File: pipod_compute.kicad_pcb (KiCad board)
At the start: 4 copper layers, 55.5 x 84.8 mm, 37 parts, among them J1 Micro_SD_Card, J2 S7041-42R, J3 S7041-42R, J5 2-1734839-5

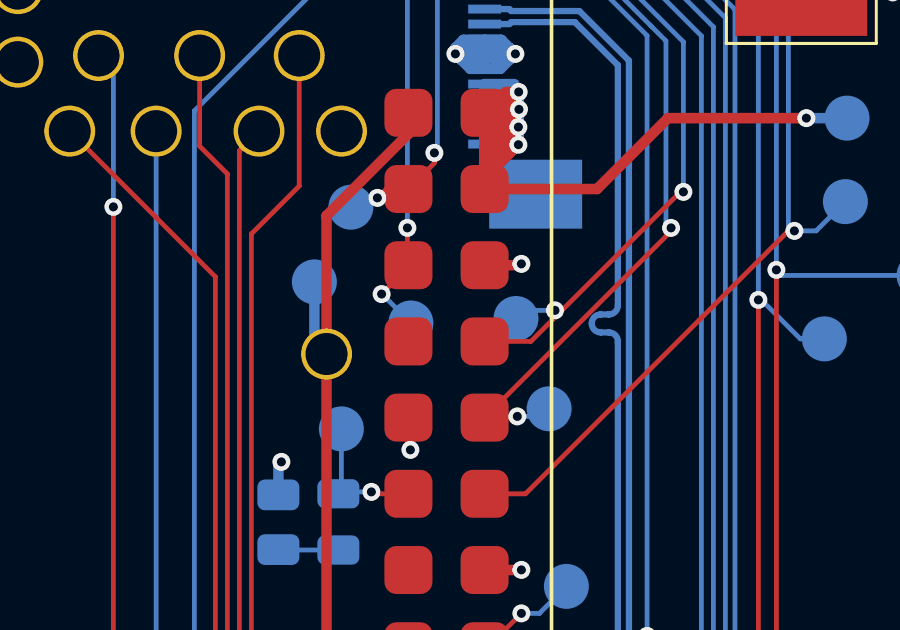
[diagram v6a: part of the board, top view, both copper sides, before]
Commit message: compute: fill out bom columns
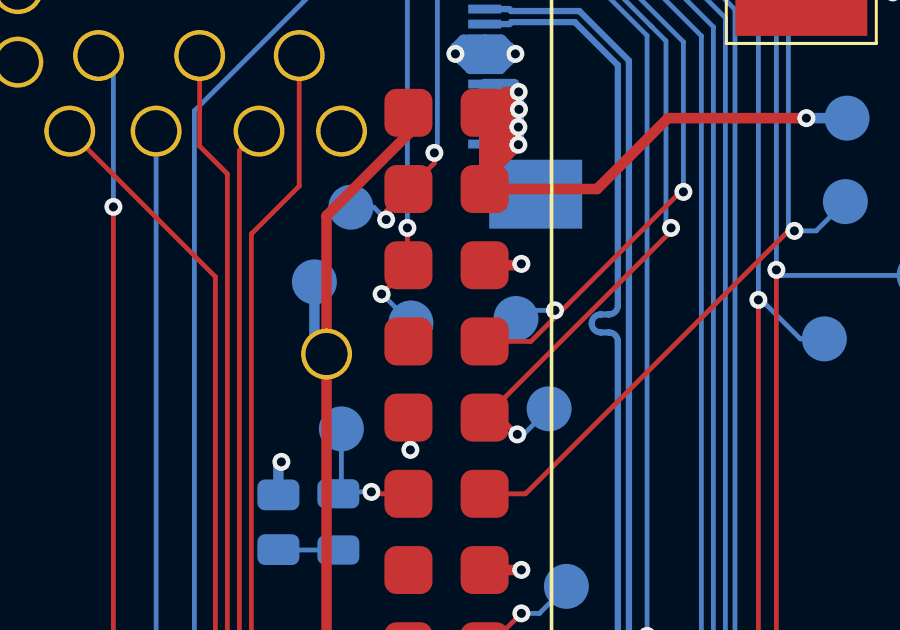
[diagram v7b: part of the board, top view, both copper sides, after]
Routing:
- net SMC_PI_I2C_SDA: track 11.6 -> 12.1 mm
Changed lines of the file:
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@@
   (segment (start 35.59 37.65) (end 35.32 37.92) (width 0.16) (layer "B.Cu") (net 41))
   (segment (start 40.9 28.7) (end 38.307 26.107) (width 0.16) (layer "B.Cu") (net 41))
+  (segment (start 35.364 41.783) (end 34.806 41.225) (width 0.16) (layer "F.Cu") (net 42))
   (segment (start 40.4895 34.9) (end 40.4895 35.0105) (width 0.16) (layer "F.Cu") (net 42))
-  (segment (start 34.275 41.225) (end 35.323 41.225) (width 0.16) (layer "F.Cu") (net 42))
   (segment (start 40.4895 35.0105) (end 34.275 41.225) (width 0.16) (layer "F.Cu") (net 42))
-  (segment (start 35.323 41.225) (end 35.364 41.184) (width 0.16) (layer "F.Cu") (net 42))
+  (segment (start 34.806 41.225) (end 34.275 41.225) (width 0.16) (layer "F.Cu") (net 42))
   (via (at 40.4895 34.9) (size 0.6) (drill 0.3) (layers "F.Cu" "B.Cu") (net 42))
-  (via (at 35.364 41.184) (size 0.6) (drill 0.3) (layers "F.Cu" "B.Cu") (net 42))
+  (via (at 35.364 41.783) (size 0.6) (drill 0.3) (layers "F.Cu" "B.Cu") (net 42))
   (segment (start 40.31952 28.667651) (end 39.825935 28.174065) (width 0.16) (layer "B.Cu") (net 42))
-  (segment (start 35.364 41.184) (end 36.171 41.184) (width 0.16) (layer "B.Cu") (net 42))
+  (segment (start 35.364 41.783) (end 35.572 41.783) (width 0.16) (layer "B.Cu") (net 42))
   (segment (start 40.31952 34.73002) (end 40.31952 28.667651) (width 0.16) (layer "B.Cu") (net 42))
   (segment (start 40.4895 34.9) (end 40.31952 34.73002) (width 0.16) (layer "B.Cu") (net 42))
   (segment (start 38.25887 26.607) (end 34.275 26.607) (width 0.16) (layer "B.Cu") (net 42))
-  (segment (start 36.171 41.184) (end 36.425 40.93) (width 0.16) (layer "B.Cu") (net 42))
   (segment (start 39.825935 28.174065) (end 38.25887 26.607) (width 0.16) (layer "B.Cu") (net 42))
-  (segment (start 30.7 33.9) (end 30.995 33.605) (width 0.16) (layer "F.Cu") (net 43))
+  (segment (start 35.572 41.783) (end 36.425 40.93) (width 0.16) (layer "B.Cu") (net 42))
   (segment (start 32.6 32.4) (end 32.6 32.74) (width 0.16) (layer "F.Cu") (net 43))
-  (segment (start 30.995 33.605) (end 31.735 33.605) (width 0.16) (layer "F.Cu") (net 43))
+  (segment (start 30.992754 34.623147) (end 30.992754 34.347246) (width 0.16) (layer "F.Cu") (net 43))
+  (segment (start 30.992754 34.347246) (end 31.735 33.605) (width 0.16) (layer "F.Cu") (net 43))
   (segment (start 32.6 32.74) (end 31.735 33.605) (width 0.16) (layer "F.Cu") (net 43))
   (via (at 32.6 32.4) (size 0.6) (drill 0.3) (layers "F.Cu" "B.Cu") (net 43))
-  (via (at 30.7 33.9) (size 0.6) (drill 0.3) (layers "F.Cu" "B.Cu") (net 43))
-  (segment (start 30.7 33.9) (end 30.127 33.9) (width 0.16) (layer "B.Cu") (net 43))
-  (segment (start 30.127 33.9) (end 29.816 34.211) (width 0.16) (layer "B.Cu") (net 43))
+  (via (at 30.992754 34.623147) (size 0.6) (drill 0.3) (layers "F.Cu" "B.Cu") (net 43))
+  (segment (start 30.580607 34.211) (end 29.816 34.211) (width 0.16) (layer "B.Cu") (net 43))
   (segment (start 32.7 32.3) (end 32.6 32.4) (width 0.16) (layer "B.Cu") (net 43))
   (segment (start 32.7 26.472) (end 32.7 32.2) (width 0.16) (layer "B.Cu") (net 43))
+  (segment (start 30.992754 34.623147) (end 30.580607 34.211) (width 0.16) (layer "B.Cu") (net 43))
   (segment (start 33.565 25.607) (end 32.7 26.472) (width 0.16) (layer "B.Cu") (net 43))
   (segment (start 32.7 32.2) (end 32.7 32.3) (width 0.16) (layer "B.Cu") (net 43))

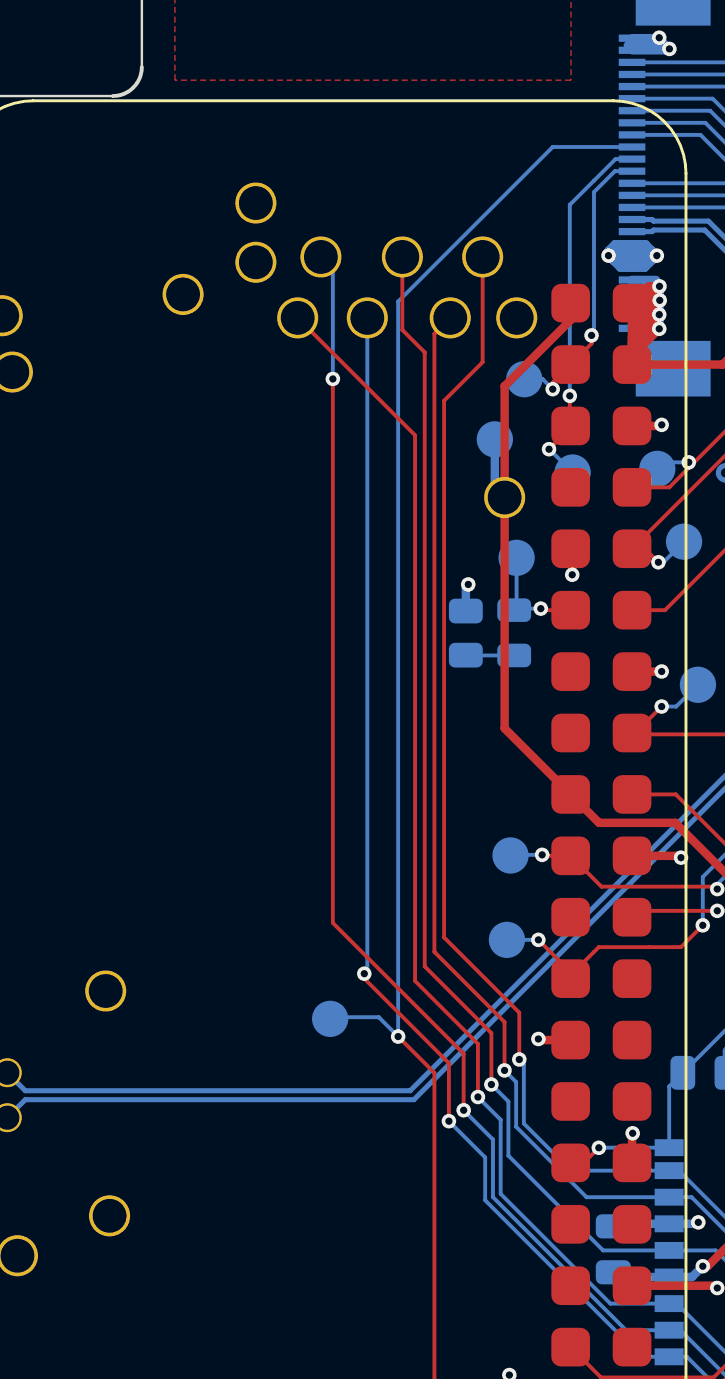
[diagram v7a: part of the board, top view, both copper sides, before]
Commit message: feature: add hardware ID resistors
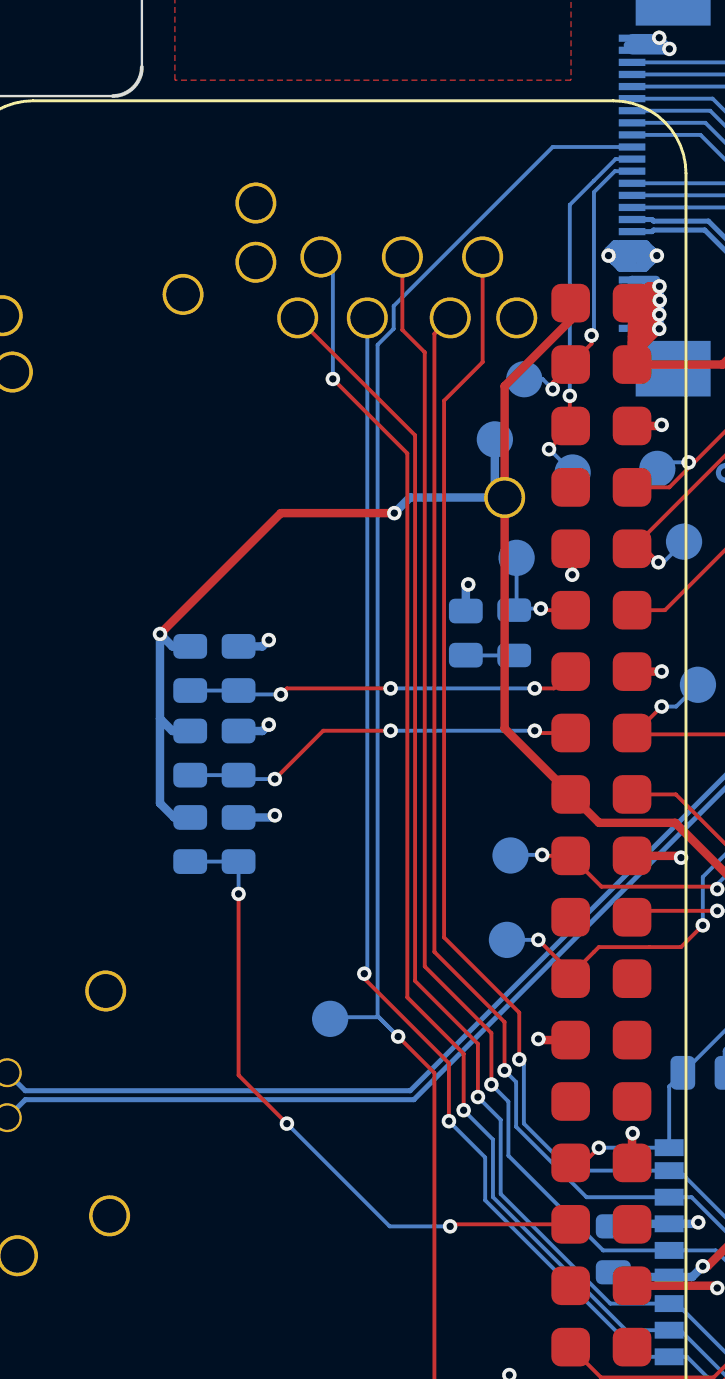
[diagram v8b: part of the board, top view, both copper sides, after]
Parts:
- added R3: DNI, Resistor_SMD:R_0805_2012Metric, B.Cu at (16.0, 53.2)
- added R4: 10k, Resistor_SMD:R_0805_2012Metric, B.Cu at (18.0, 53.2)
- added R5: DNI, Resistor_SMD:R_0805_2012Metric, B.Cu at (16.0, 49.7)
- added R6: 10k, Resistor_SMD:R_0805_2012Metric, B.Cu at (18.0, 49.7)
- added R7: DNI, Resistor_SMD:R_0805_2012Metric, B.Cu at (16.0, 46.2)
- added R8: 10k, Resistor_SMD:R_0805_2012Metric, B.Cu at (18.0, 46.2)
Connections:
- A1 pad 13: unconnected-(A1-Pad13) -> HWID2
- A1 pad 15: unconnected-(A1-Pad15) -> HWID1
- A1 pad 31: unconnected-(A1-Pad31) -> HWID0
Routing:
- net +3V3: track 55.3 -> 83.3 mm, vias 2 -> 4
- net HWID0: track 0.00 -> 27.2 mm, vias 0 -> 3
- net HWID1: track 0.00 -> 16.7 mm, vias 0 -> 3
- net HWID2: track 0.00 -> 16.2 mm, vias 0 -> 3
- net GND: track 53.9 -> 58.1 mm, vias 23 -> 26
- net HP_SL_VIDEO: track 62.2 -> 62.9 mm
